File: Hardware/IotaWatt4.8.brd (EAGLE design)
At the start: 80 x 113 mm, 59 parts, among them J0 2.1MMJACKSMT, J1 STEREO_SMD, J10 STEREO_SMD, J11 STEREO_SMD, J12 STEREO_SMD, J13 STEREO_SMD, J14 STEREO_SMD, J2 STEREO_SMD, J3 STEREO_SMD, J4 STEREO_SMD, J5 STEREO_SMD, J6 STEREO_SMD, J7 STEREO_SMD, J8 STEREO_SMD, J9 STEREO_SMD, Y1 32Khz

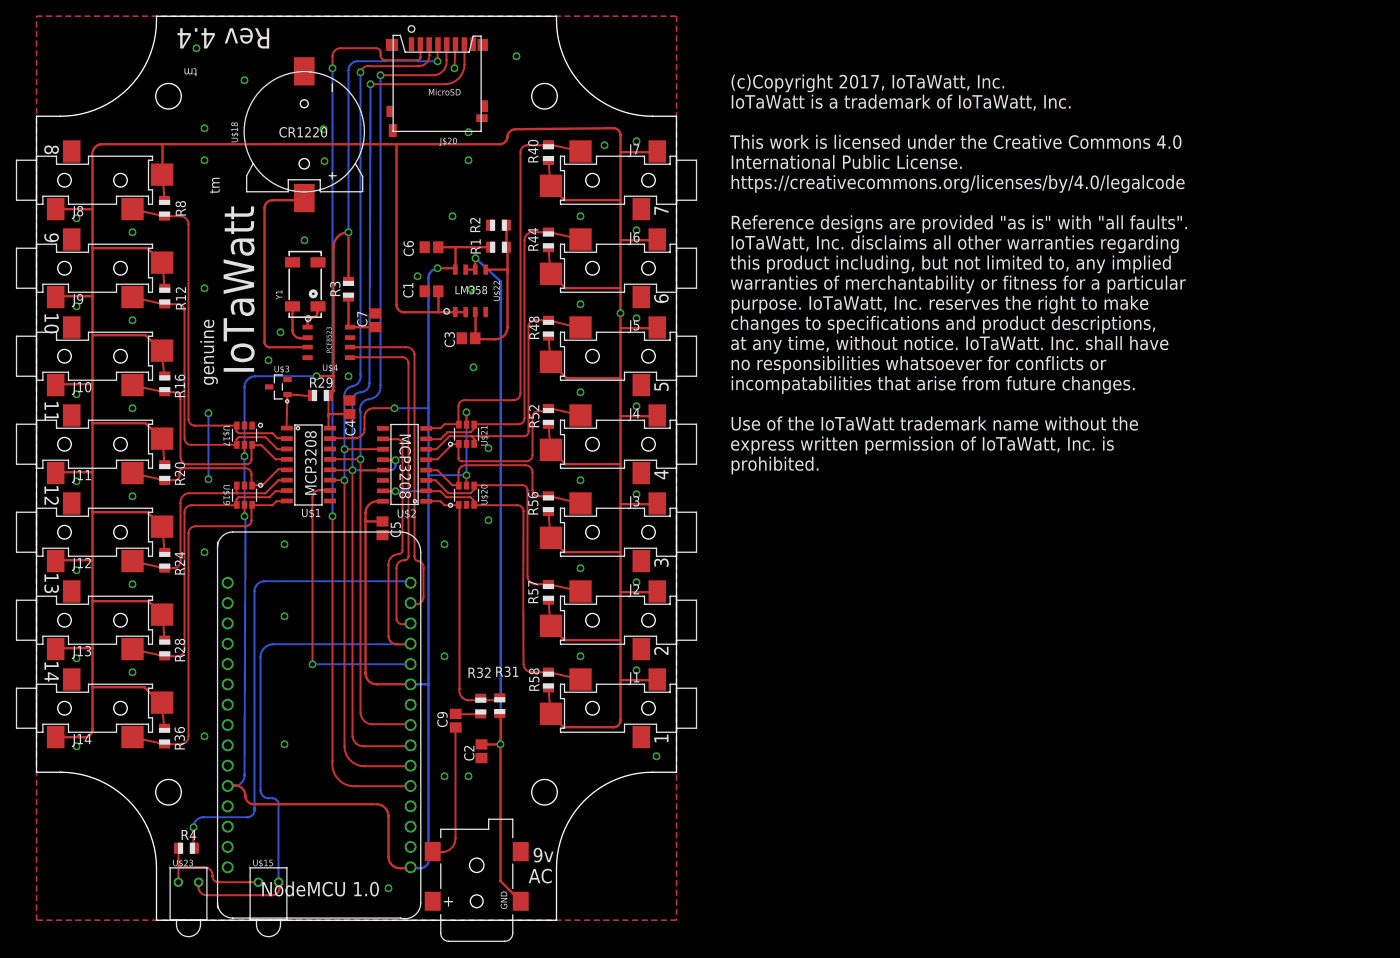
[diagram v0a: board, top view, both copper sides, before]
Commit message: Update to latest version 4.8
Remove extra LED mounting position
Reroute traces around SDcard to eliminate mfg problems
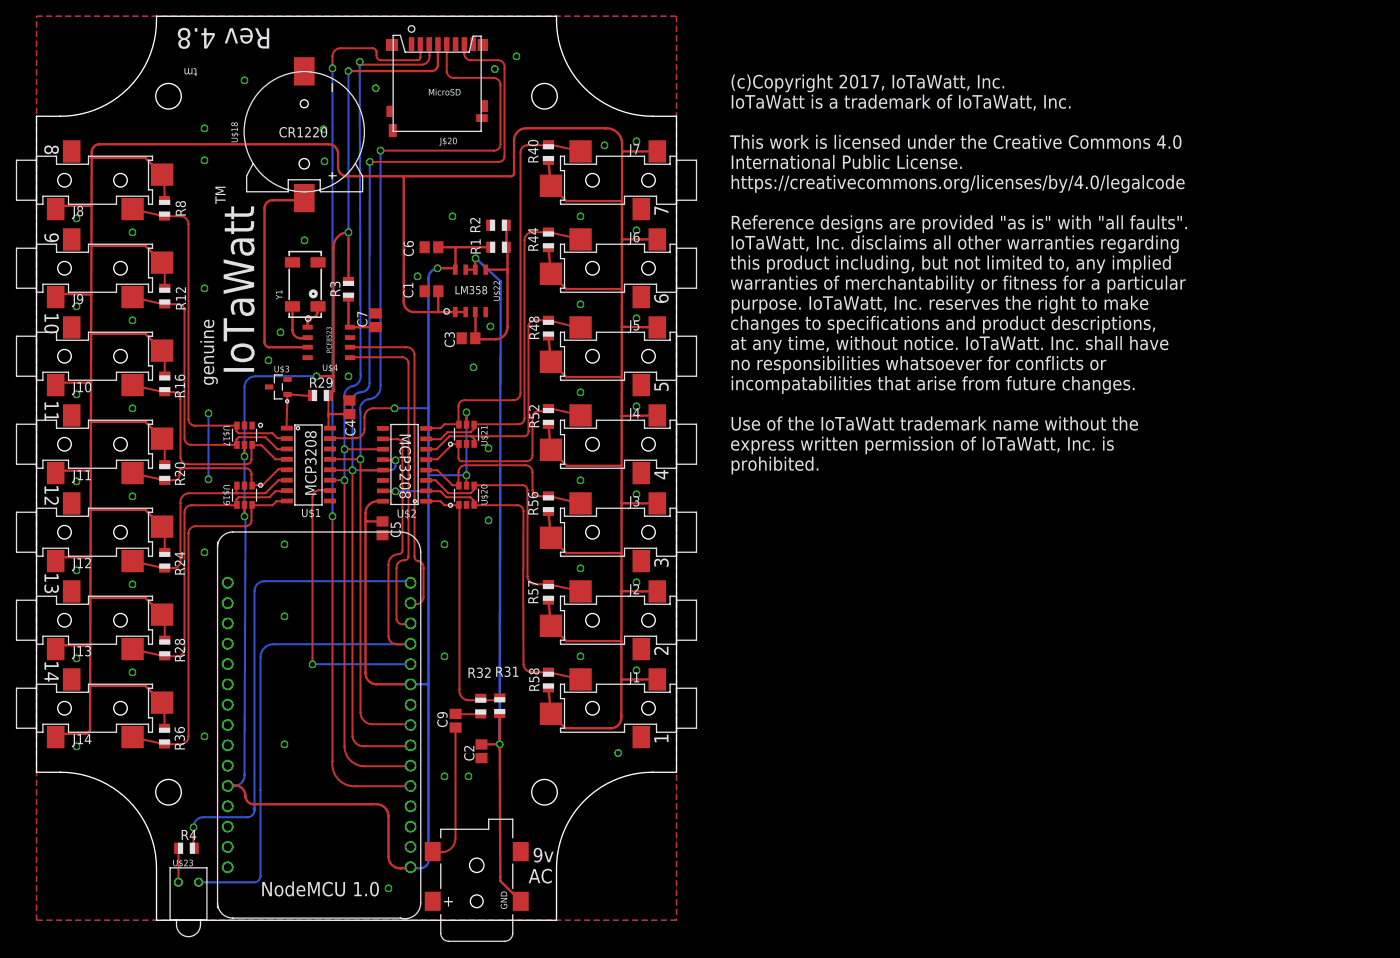
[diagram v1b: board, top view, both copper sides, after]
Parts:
- removed U$15: LED_RT_TRH, IotaWatt_parts:LED_TH_RT
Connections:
- net ADCCS1: no longer U$15.P$1
- net N$8: no longer U$15.P$2
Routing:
- net SCLK: track 105.2 -> 118.1 mm
- net N$8: track 15.0 -> 4.12 mm
- net MISO: track 116.2 -> 126.4 mm
- net BIAS: track 481.8 -> 490.1 mm, vias 1 -> 0
- net ADCCS1: track 92.2 -> 85.8 mm
- net GND: track 11.4 -> 8.43 mm, vias 61 -> 59
- net MOSI: track 111.0 -> 112.3 mm
- net ACBIAS: track 92.1 -> 91.5 mm
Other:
- board text added: "Rev 4.8"
- board text added: "TM"
- board text removed: "Rev 4.4"
